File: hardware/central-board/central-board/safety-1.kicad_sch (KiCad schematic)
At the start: 20 parts, among them J401 TBD E-stop 4pin, J402 TBD 2pin, J403 TBD 2pin, Q401 IRLML0100TRPBF, U401 LTV-817S, U402 SN74AHCT1G125DBVR, X402 RETURN JOIN TBD

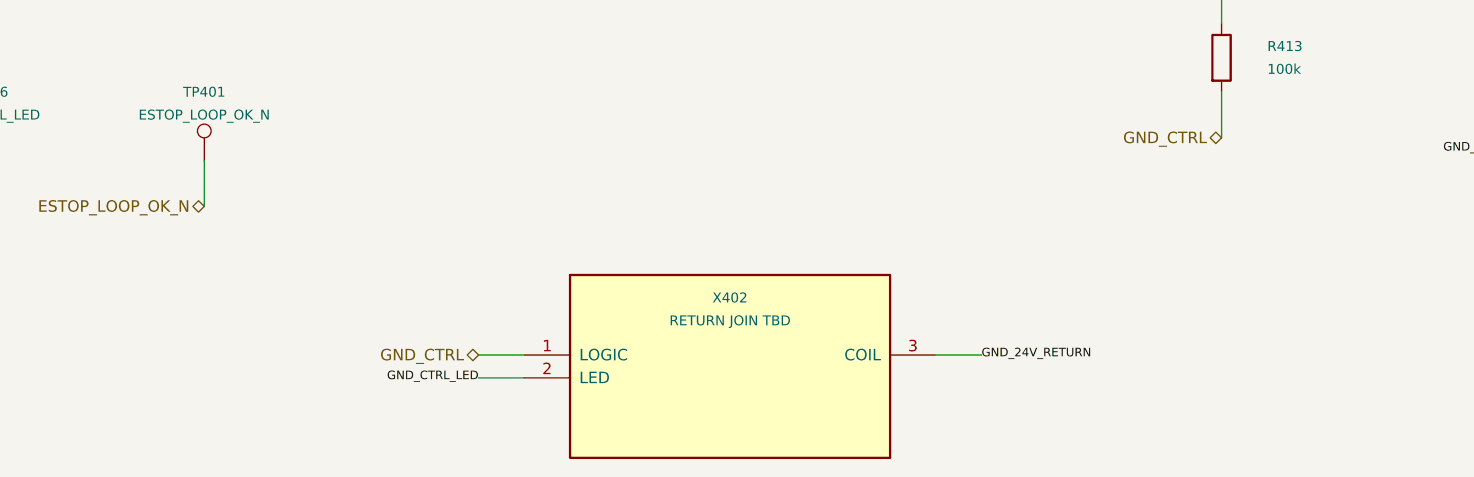
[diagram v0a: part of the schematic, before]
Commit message: Select X402 ground net tie and save central board updates
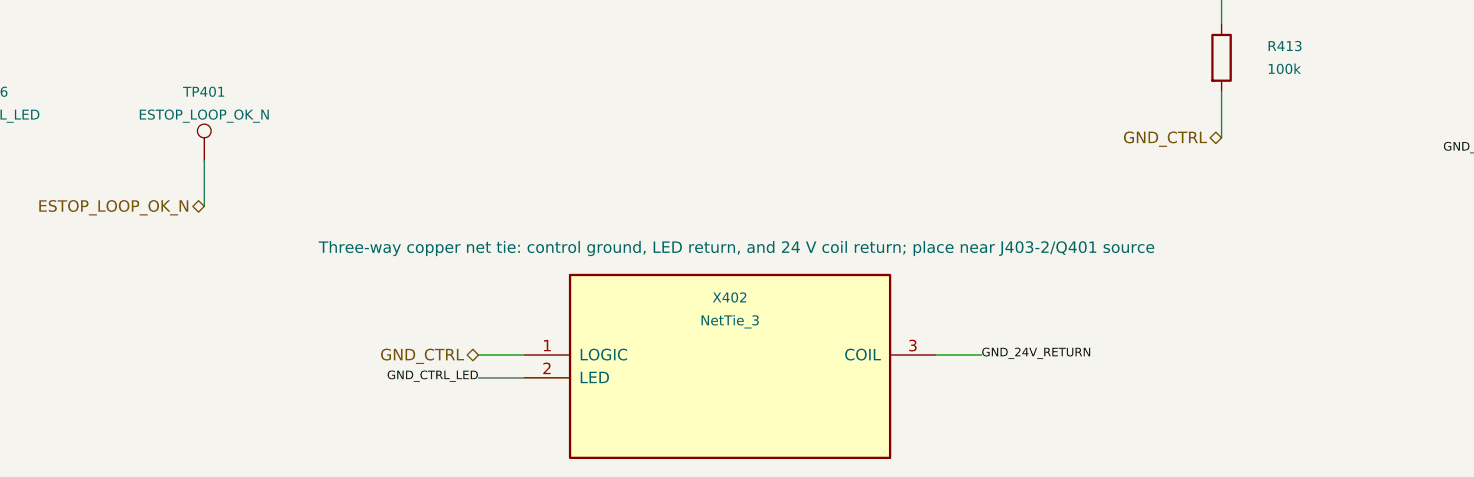
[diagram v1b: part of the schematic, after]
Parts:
- J401: footprint (none) -> Connector_JST:JST_XH_S4B-XH-A_1x04_P2.50mm_Horizontal
- X402: value RETURN JOIN TBD -> NetTie_3; footprint (none) -> NetTie:NetTie-3_SMD_Pad2.0mm; Design status TBD functional placeholder; no selected device or conductiv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 -> Selected copper net tie; no purchased component. PCB placem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; now left out of the parts list
